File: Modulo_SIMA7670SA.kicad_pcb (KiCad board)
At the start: 2 copper layers, 100 x 78 mm, 58 parts, among them J1 TBP01R1-508-02BE, J2 DB9 Hembra Impreso 90°, J3 U.FL IPEX1 MALE, J4 SMA-J-P-X-RA-TH1, J5 Jack DC 2.1mm PCB recto, Q1 BSS138, Q2 FDN340P, Q3 FDN340P, Q4 BSS138, U1 MAX232, U2 24LC512, U3 BKP-A7670SA (Módulo SIMCOM), U4 MAX706, U5 Black_Pill_STM32F411CEUx, U6 LM2596S_Modulo_Regulable, U7 LM7805_TO220

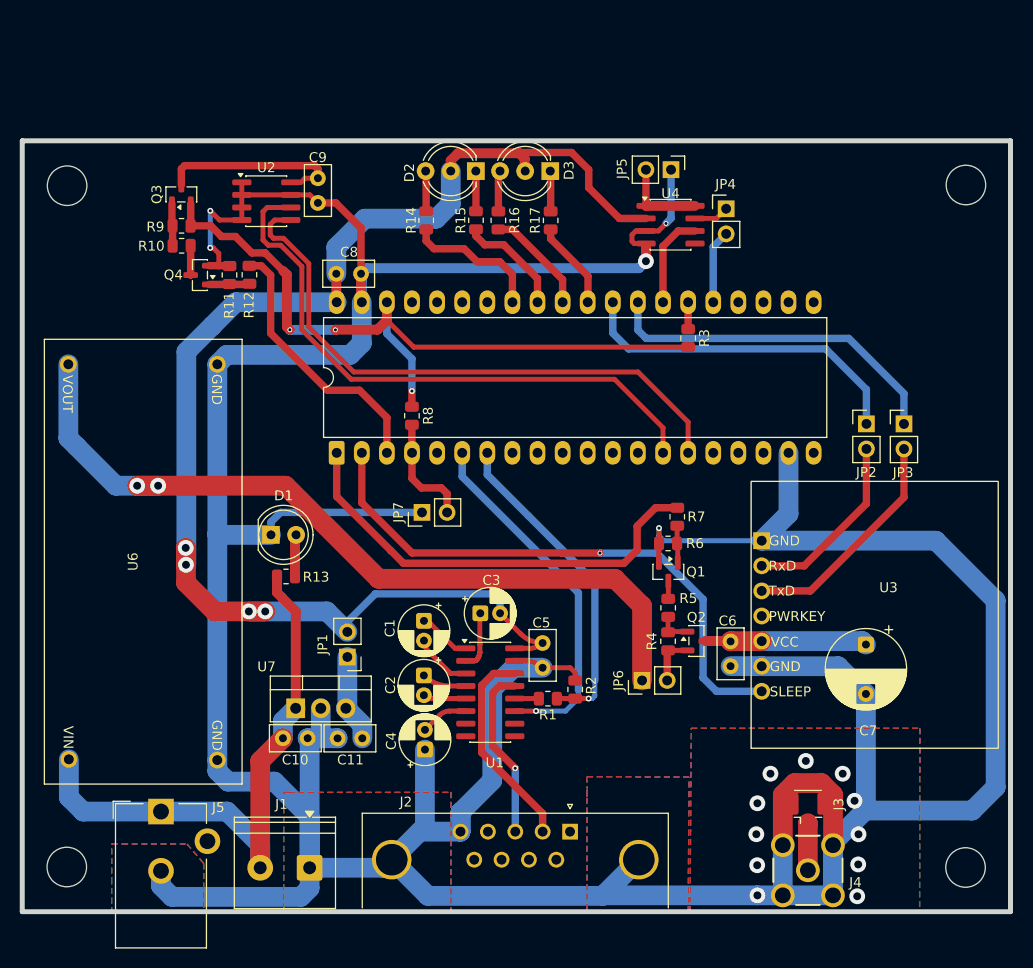
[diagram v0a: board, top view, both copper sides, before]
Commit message: Estamos haciendo un nuevo PCB porque se hicieron mpodificaciones en el circuito eléctrico para manejar la señal de ON/OFF del BKP-A7670SA en el riel de los 12V.
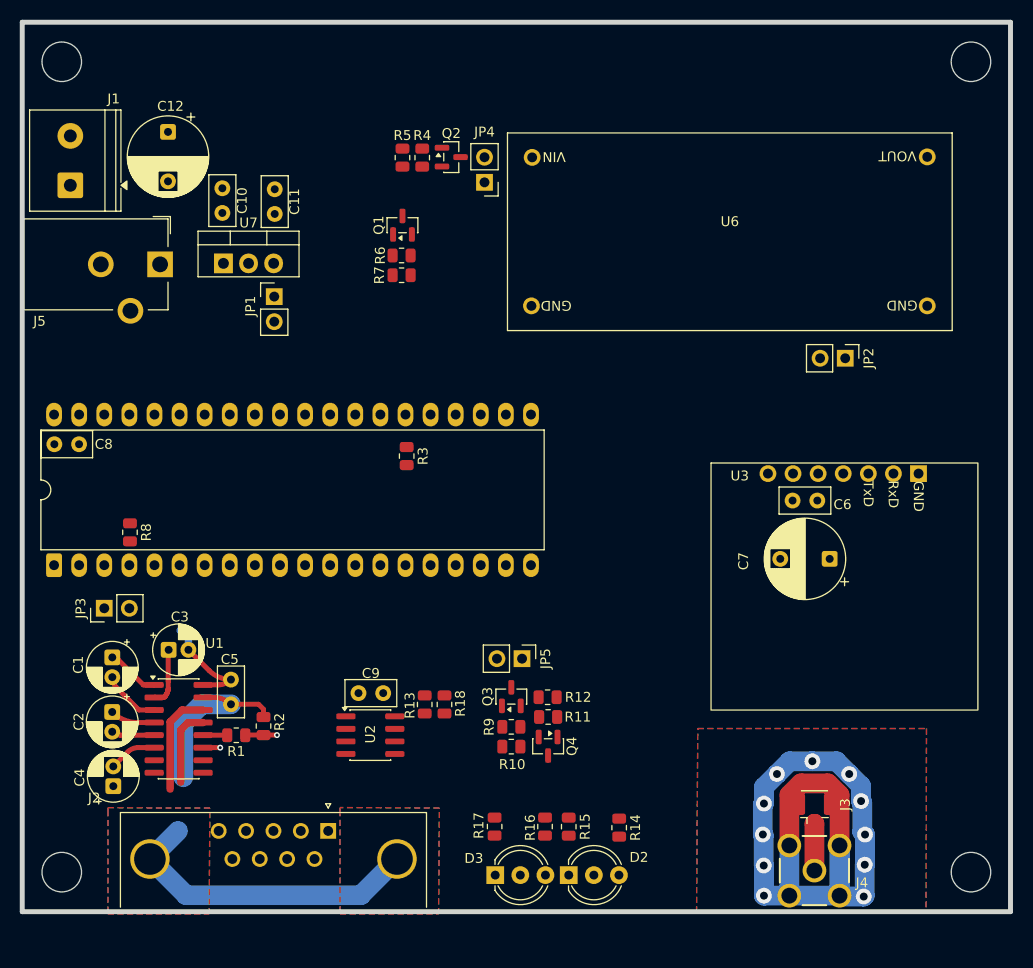
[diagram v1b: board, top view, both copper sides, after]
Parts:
- removed D1: LED Rojo 5mm, LED_THT:LED_D5.0mm
- removed JP6: Jumper_2_Open, Connector_PinHeader_2.54mm:PinHeader_1x02_P2.54mm_Vertical
- removed JP7: Config/Normal, Connector_PinHeader_2.54mm:PinHeader_1x02_P2.54mm_Vertical
- removed U4: MAX706, Package_SO:SOIC-8_3.9x4.9mm_P1.27mm
- added C12: 1000uF, Capacitor_THT:CP_Radial_D8.0mm_P5.00mm, F.Cu at (129.6, 66.8)
- added R18: 4K7, Resistor_SMD:R_0805_2012Metric, F.Cu at (157.6, 124.7)
- C7: value 1000uF -> 470uF
- JP3: value Jumper_2_Open -> Config/Normal
- R10: value 10K -> 3K3
- R4, R9: value 4K7 -> 10K
- R5: value 10K -> 15K
- moved JP3 83.0 mm to (123.2, 115.0), turned to 90 degrees
- moved J1 73.2 mm to (119.7, 72.2), turned to 90 degrees
- moved D2 71.9 mm to (170.2, 142.0), turned to 0 degrees
- moved D3 71.5 mm to (162.7, 142.0), turned to 0 degrees
- moved U6 68.1 mm to (186.5, 76.9), turned to 180 degrees
- moved R14 64.5 mm to (175.3, 137.2), turned to -90 degrees
- moved R15 62.1 mm to (170.2, 137.1), turned to -90 degrees
- moved R17 61.6 mm to (162.7, 137.0), turned to -90 degrees
- moved R16 61.5 mm to (167.8, 137.0), turned to -90 degrees
- moved Q3 60.8 mm to (164.3, 123.9)
- moved R9 60.7 mm to (164.3, 127.0)
- moved R10 60.7 mm to (164.3, 129.0)
- moved Q4 59.3 mm to (168.1, 128.9), turned to -90 degrees
- moved J5 55.4 mm to (128.8, 80.2), turned to -90 degrees
- moved R11 55.1 mm to (168.1, 126.0), turned to 180 degrees
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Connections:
- JP2 pad 2: UART2_RX -> 5V_MODEM
- JP3 pad 1: Net-(JP3-A) -> GND
- JP3 pad 2: UART2_TX -> Net-(JP3-B)
- JP4 pad 1: Net-(JP4-A) -> +12V
- JP4 pad 2: NRST -> 12V_StepDown
- JP5 pad 1: GND -> 3V3
- JP5 pad 2: Net-(JP5-B) -> 3V3_MEM
- Q2 pad 2: 5V_SWITCHING -> +12V
- Q2 pad 3: 5V_MODEM -> 12V_StepDown
- R13 pad 1: +12V -> 3V3_MEM
- R13 pad 2: Net-(D1-A) -> SCL I2C1
- R4 pad 1: 5V_SWITCHING -> +12V
- R8 pad 2: Net-(JP7-B) -> Net-(JP3-B)
- U3 pad 4: UART2_TX -> UART2_RX
- U3 pad 5: UART2_RX -> UART2_TX
- U5 pad 1: ON_MODEM -> unconnected-(U5-PB12-Pad1)
- U5 pad 16: unconnected-(U5-PB8-Pad16) -> ON_MEM
- U5 pad 17: unconnected-(U5-PB9-Pad17) -> SLEEP_MODEM
- U5 pad 18: unconnected-(U5-5V-Pad18) -> +5V
- U5 pad 2: SLEEP_MODEM -> unconnected-(U5-PB13-Pad2)
- U5 pad 20: unconnected-(U5-3V3-Pad20) -> 3V3
- U5 pad 25: NRST -> unconnected-(U5-~{NRST}-Pad25)
- U5 pad 27: WDT PULSE -> ON_MODEM
- U5 pad 28: Net-(JP3-A) -> UART2_TX
- U5 pad 29: Net-(JP2-A) -> UART2_RX
- U5 pad 3: ON_MEM -> unconnected-(U5-PB14-Pad3)
- U5 pad 4: Net-(JP7-B) -> Net-(JP3-B)
- U6 pad 1: +12V -> 12V_StepDown
- U6 pad 4: Net-(JP6-A) -> Net-(JP2-A)
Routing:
- net GND: track 475.3 -> 126.7 mm, vias 16 -> 11
- net +5V: track 139.6 -> 10.7 mm, vias 4 -> 0
- net Net-(JP6-A): track 82.2 -> 0.00 mm, vias 2 -> 0
- net 3V3: track 75.0 -> 0.00 mm, vias 3 -> 0
- net SCL I2C1: track 60.5 -> 0.00 mm
- net SDA I2C1: track 60.3 -> 0.00 mm
- net +12V: track 59.3 -> 0.00 mm
- net SLEEP_MODEM: track 58.1 -> 0.00 mm, vias 1 -> 0
- net ON_MODEM: track 45.5 -> 0.00 mm
- net Net-(JP3-A): track 35.5 -> 0.00 mm
- net UART1_TX: track 36.7 -> 1.74 mm
- net Net-(JP2-A): track 34.6 -> 0.00 mm
- net UART1_RX: track 33.1 -> 3.21 mm
- net ON_MEM: track 27.3 -> 0.00 mm
- net UART2_TX: track 23.2 -> 0.00 mm
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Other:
- board size 100 x 78 mm -> 100 x 90 mm
- board text removed: "GND"

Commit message: Adelantando algo del PCB. Fue ncesario modificar GPIOs del STM32 y renombrar rieles de 3.3V; 5V; y GND, para que no tengamos líneas sin rutear.
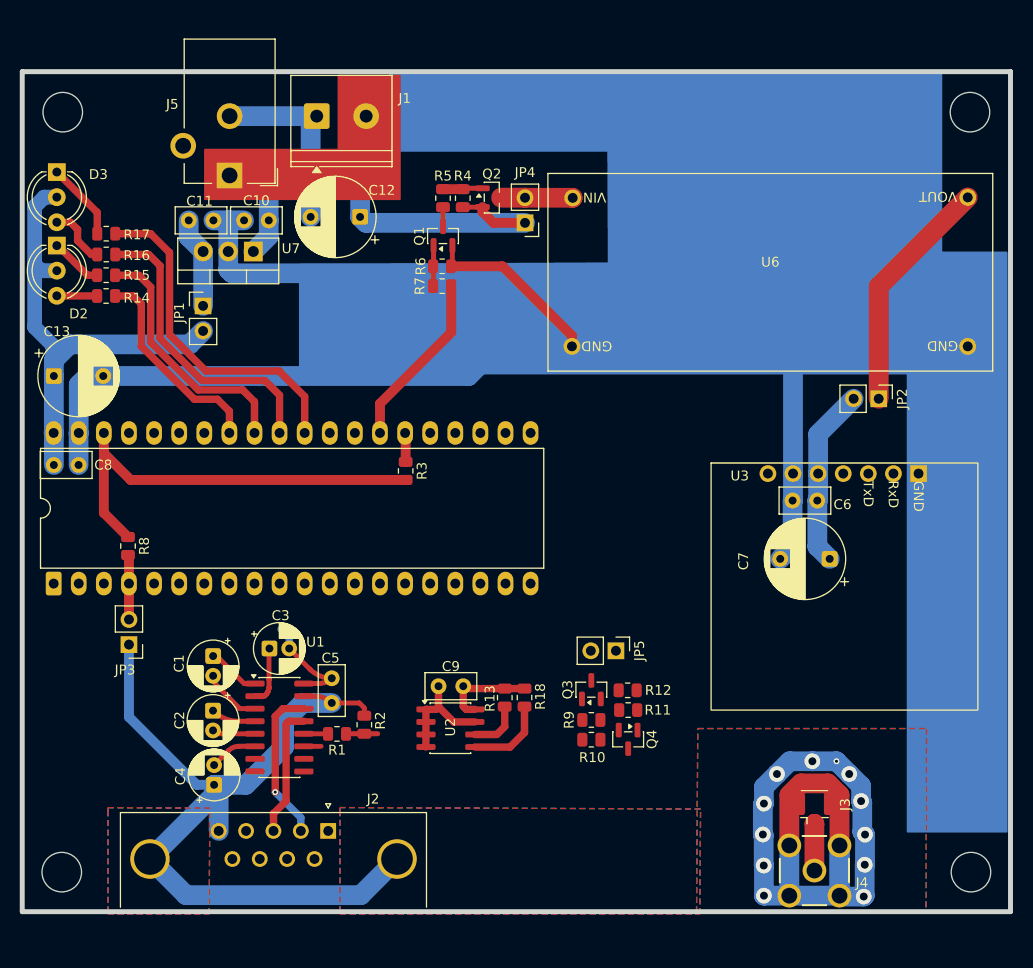
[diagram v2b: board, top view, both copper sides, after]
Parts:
- added C13: 470uF, Capacitor_THT:CP_Radial_D8.0mm_P5.00mm, F.Cu at (118.1, 91.5)
- moved D3 83.8 mm to (118.4, 70.8), turned to -90 degrees
- moved D2 82.1 mm to (118.4, 78.3), turned to -90 degrees
- moved R14 74.8 mm to (123.3, 83.4), turned to 180 degrees
- moved R16 73.0 mm to (123.4, 79.2), turned to 180 degrees
- moved R15 72.8 mm to (123.3, 81.3), turned to 180 degrees
- moved R17 71.7 mm to (123.4, 77.1), turned to 180 degrees
- moved J1 25.9 mm to (144.7, 65.2), turned to 0 degrees
- moved C12 21.3 mm to (149.0, 75.4), turned to 180 degrees
- moved J5 11.4 mm to (135.8, 71.2), turned to 180 degrees
- moved C1 10.2 mm to (134.2, 119.8)
- moved C5 10.2 mm to (146.2, 122.0)
- moved R1 10.2 mm to (146.7, 127.7)
- moved C4 10.2 mm to (134.3, 132.8)
- moved C2 10.2 mm to (134.2, 125.3)
- moved C3 10.2 mm to (139.9, 119.0)
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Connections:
- JP5 pad 1: 3V3 -> 3V3_b
- Q3 pad 2: 3V3 -> 3V3_b
- R9 pad 1: 3V3 -> 3V3_b
- U5 pad 20: 3V3 -> 3V3_b
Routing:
- net GND: track 126.7 -> 361.3 mm, vias 11 -> 12
- net +5V: track 10.7 -> 60.7 mm
- net +12V: track 0.00 -> 46.1 mm
- net 3V3: track 0.00 -> 43.2 mm
- net Net-(U5-PA4): track 0.00 -> 34.5 mm
- net Net-(U5-PA5): track 0.00 -> 30.6 mm
- net Net-(U5-PA6): track 0.00 -> 25.8 mm
- net Net-(JP2-A): track 0.00 -> 24.1 mm
- net Net-(U5-PA7): track 0.00 -> 21.1 mm
- net 5V_MODEM: track 0.00 -> 18.2 mm
- net ON_MODEM: track 0.00 -> 17.8 mm
- net 3V3_MEM: track 0.00 -> 9.64 mm
- net Net-(JP1-A): track 0.00 -> 9.26 mm
- net SDA I2C1: track 0.00 -> 8.26 mm
- net Net-(D3-K1): track 0.00 -> 8.02 mm
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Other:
- board size 100 x 90 mm -> 100 x 85 mm

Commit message: Se va avanzando con el PCB. Sin enrutar "17".
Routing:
- net +5V: track 60.7 -> 79.5 mm
- net Net-(Q3-G): track 0.00 -> 4.14 mm
- net Net-(Q4-G): track 0.00 -> 4.06 mm
- net Net-(Q4-D): track 0.00 -> 3.19 mm
- net 3V3_MEM: track 9.64 -> 12.7 mm
- net 3V3_b: track 0.00 -> 2.14 mm
- net GND: track 361.3 -> 363.3 mm
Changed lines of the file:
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@@
+	)
+	(segment
+		(start 172.4475 122.26)
+		(end 172.4475 119.3125)
+		(width 0.75)
+		(layer "F.Cu")
+		(net "3V3_MEM")
 	)
 	(segment
@@
 		(start 159.79 125.19)
 		(end 159.485 124.885)
+		(width 0.75)
+		(layer "F.Cu")
+		(net "3V3_MEM")
+	)
+	(segment
+		(start 172.4475 119.3125)
+		(end 172.395 119.26)
 		(width 0.75)
 		(layer "F.Cu")
@@
 	)
 	(segment
+		(start 175.2225 125.2975)
+		(end 175.26 125.26)
+		(width 0.75)
+		(layer "F.Cu")
+		(net "GND")
+	)
+	(segment
 		(start 158.385 80.235)
 		(end 158.26 80.36)
@@
 		(end 158.385 80.235)
 		(width 0.5)
+		(layer "F.Cu")
+		(net "GND")
+	)
+	(segment
+		(start 175.2225 127.285)
+		(end 175.2225 125.2975)
+		(width 0.75)
 		(layer "F.Cu")
 		(net "GND")
@@
 	)
 	(segment
+		(start 161.22 116.1)
+		(end 158.26 119.06)
+		(width 1.5)
+		(layer "B.Cu")
+		(net "+5V")
+	)
+	(segment
 		(start 131.8 88.26)
 		(end 119.66 88.26)
@@
 	)
 	(segment
-		(start 141.874888 119.03)
-		(end 141.874888 117.89863)
-		(width 0.75)
+		(start 149.16 119.06)
+		(end 146.18 122.04)
+		(width 1.5)
 		(layer "B.Cu")
 		(net "+5V")
@@
 	)
 	(segment
+		(start 161.22 112.46)
+		(end 161.22 116.1)
+		(width 1.5)
+		(layer "B.Cu")
+		(net "+5V")
+	)
+	(segment
 		(start 118.06 91.46)
 		(end 117.96 91.36)
@@
 	)
 	(segment
-		(start 141.874888 117.89863)
-		(end 141.041258 117.065)
-		(width 0.75)
+		(start 158.26 119.06)
+		(end 149.16 119.06)
+		(width 1.5)
 		(layer "B.Cu")
 		(net "+5V")
@@
 		(layer "F.Cu")
 		(net "Net-(U1-VS-)")
+	)
+	(segment
+		(start 171.4975 126.2225)
+		(end 171.535 126.26)
+		(width 0.75)
+		(layer "F.Cu")
+		(net "Net-(Q3-G)")
+	)
+	(segment
+		(start 171.535 128.26)
+		(end 171.535 126.26)
+		(width 0.75)
+		(layer "F.Cu")
+		(net "Net-(Q3-G)")
+	)
+	(segment
+		(start 171.4975 124.135)
+		(end 171.4975 126.2225)
+		(width 0.75)
+		(layer "F.Cu")
+		(net "Net-(Q3-G)")
 	)
 	(segment
@@
 	)
 	(segment
-		(start 125.66 116.16)
-		(end 125.66 112.46)
-		(width 1)
-		(layer "F.Cu")
-		(net "Net-(JP3-B)")
-	)
-	(segment
 		(start 125.66 112.46)
 		(end 125.66 109.6725)
@@
 	)
 	(segment
+		(start 125.66 116.095)
+		(end 125.66 112.46)
+		(width 0.75)
+		(layer "B.Cu")
+		(net "Net-(JP3-B)")
+	)
+	(segment
 		(start 145.095 128.93)
 		(end 143.36 128.93)
@@
 		(layer "F.Cu")
 		(net "Net-(U1-VS+)")
+	)
+	(segment
+		(start 177.035 125.21)
+		(end 177.085 125.26)
+		(width 0.75)
+		(layer "F.Cu")
+		(net "Net-(Q4-G)")
+	)
+	(segment
+		(start 177.085 125.26)
+		(end 177.085 127.2475)
+		(width 0.75)
+		(layer "F.Cu")
+		(net "Net-(Q4-G)")
+	)
+	(segment
+		(start 177.035 123.26)
+		(end 177.035 125.21)
+		(width 0.75)
+		(layer "F.Cu")
+		(net "Net-(Q4-G)")
+	)
+	(segment
+		(start 177.085 127.2475)
+		(end 177.1225 127.285)
+		(width 0.75)
+		(layer "F.Cu")
+		(net "Net-(Q4-G)")
 	)
 	(segment
@@
 	)
 	(segment
+		(start 174.26 129.16)
+		(end 176.1725 129.16)
+		(width 0.75)
+		(layer "F.Cu")
+		(net "Net-(Q4-D)")
+	)
+	(segment
+		(start 173.36 128.26)
+		(end 174.26 129.16)
+		(width 0.75)
+		(layer "F.Cu")
+		(net "Net-(Q4-D)")
+	)
+	(segment
 		(start 157.435 74.3725)
 		(end 157.435 76.36)
@@
 		(net "Net-(Q1-D)")
 	)
+	(segment
+		(start 173.3975 126.2225)
+		(end 173.36 126.26)
+		(width 0.75)
+		(layer "F.Cu")
+		(net "3V3_b")
+	)
+	(segment
+		(start 173.3975 124.135)
+		(end 173.3975 126.2225)
+		(width 0.75)
+		(layer "F.Cu")
+		(net "3V3_b")
+	)
 	(zone

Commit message: Ya está todo ruteado, falta una sola net sin rutear que no se cual es. Solo hay que revisar.
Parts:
- moved R18 10.1 mm to (156.1, 120.7), turned to 0 degrees
- moved R11 9.62 mm to (175.3, 115.7)
- moved R12 9.62 mm to (175.3, 113.7)
- moved Q4 9.62 mm to (175.3, 118.6)
- moved JP5 8.63 mm to (166.3, 120.0), turned to 0 degrees
- moved R13 7.71 mm to (156.1, 122.7), turned to 0 degrees
- moved R10 6.43 mm to (175.3, 122.5), turned to 90 degrees
- moved C9 6.08 mm to (154.9, 126.9), turned to -90 degrees
- moved R9 3.84 mm to (173.3, 122.5), turned to -90 degrees
- moved JP3 3.57 mm to (128.2, 116.2), turned to -90 degrees
- moved Q3 2.27 mm to (170.3, 122.5), turned to 180 degrees
- moved U2 1.48 mm to (159.2, 128.2), turned to 90 degrees
- moved R1 0.57 mm to (146.5, 127.2)
- moved R2 0.54 mm to (149.3, 126.2)
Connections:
- C3 pad 2: +5V -> +5V_b
- C5 pad 1: +5V -> +5V_b
- J2 pad 0: (no net) -> GND
- U1 pad 16: +5V -> +5V_b
- U5 pad 18: +5V -> +5V_b
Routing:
- net GND: track 363.3 -> 441.0 mm, vias 12 -> 13
- net UART2_RX: track 0.00 -> 61.2 mm, vias 0 -> 1
- net UART2_TX: track 0.00 -> 59.9 mm, vias 0 -> 1
- net SLEEP_MODEM: track 0.00 -> 39.5 mm
- net UART1_TX: track 1.73 -> 39.9 mm, vias 0 -> 1
- net +5V_b: track 0.00 -> 30.7 mm
- net +5V: track 79.5 -> 50.0 mm
- net UART1_RX: track 3.21 -> 30.3 mm
- net ON_MEM: track 0.00 -> 20.7 mm
- net SCL I2C1: track 5.38 -> 19.2 mm, vias 0 -> 2
- net 3V3_MEM: track 12.7 -> 25.8 mm
- net 3V3_b: track 2.14 -> 15.2 mm
- net SDA I2C1: track 8.26 -> 17.9 mm
- net Net-(Q4-D): track 3.19 -> 2.04 mm

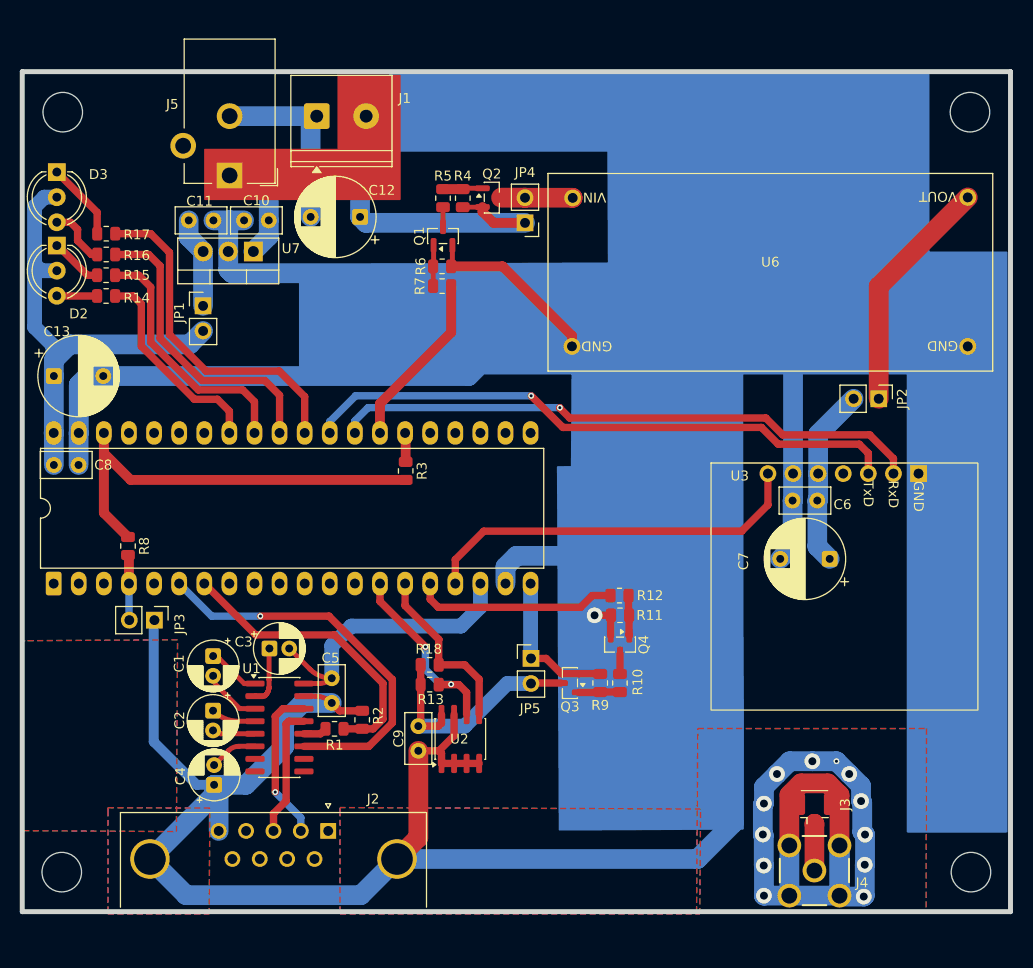
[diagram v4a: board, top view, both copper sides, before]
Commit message: fix(pcb): corregir jerarquia de prioridades en zonas de cobre
- Reordenar prioridades de las 10 zonas: potencia (+12V, Net-JP2-A)
  por debajo del plano de GND, GND en rango 4-8, zona RF_LTE_4G
  como techo absoluto en prioridad 9
- Restaurar nombre descriptivo "RF_LTE_4G" (habia quedado
  renombrada a "Pour0"/"Pour1" con uuid duplicado por error previo)
- Subir Pour3 (GND) de prioridad 1 a 4+, unico outlier que quedaba
  por debajo de los pours de potencia

Nota de diseno: se dejan documentadas 8 superposiciones de courtyard
(C6/C7-U3, C8/R3/R8-U5, D3-H2, C4-J2, C9-R13) como no criticas -
los componentes involucrados (U3, U5) montan sobre zocalo con
altura libre suficiente debajo. Excluir estas violaciones puntuales
en el DRC de KiCad (click derecho -> Exclude this violation) para
mantener el resto de las verificaciones limpias.
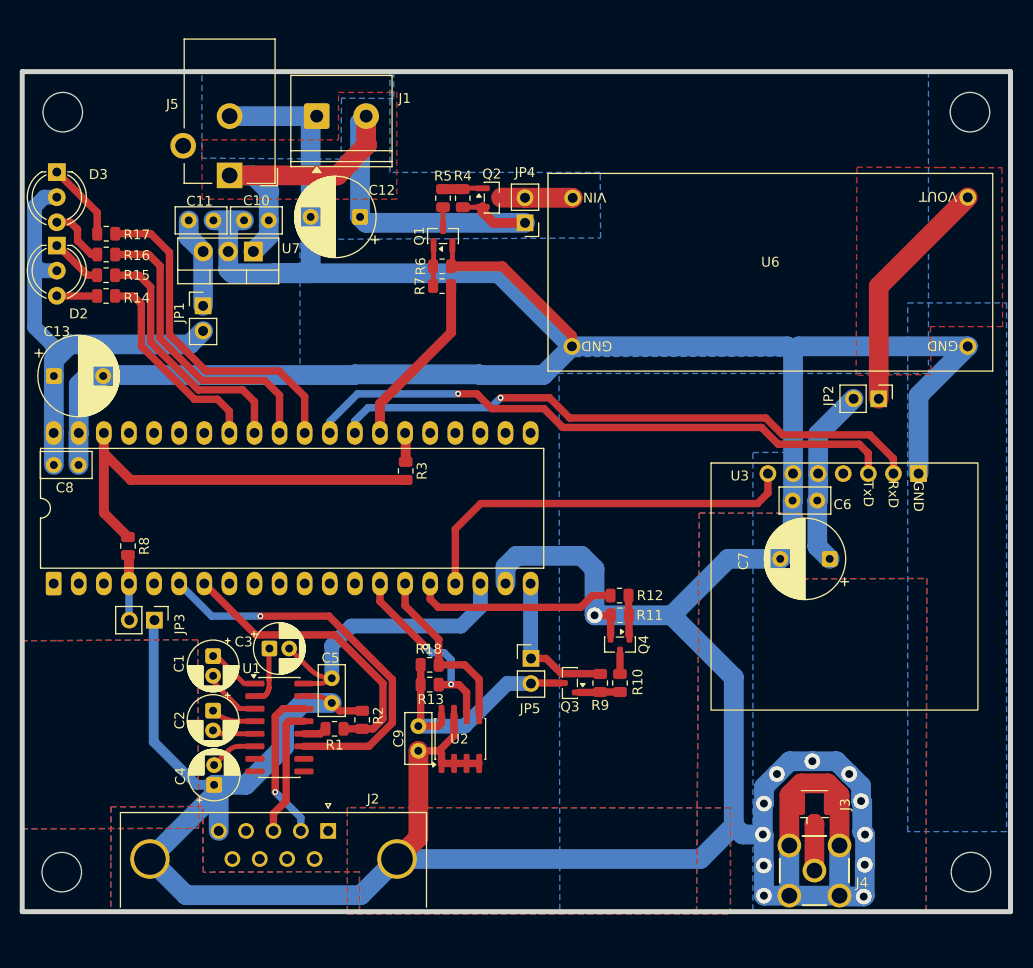
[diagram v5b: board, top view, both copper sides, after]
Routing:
- net GND: track 441.0 -> 520.4 mm, vias 13 -> 12
- net +12V: track 46.1 -> 64.3 mm
- net SLEEP_MODEM: track 39.5 -> 40.6 mm
- net UART2_TX: track 59.9 -> 60.7 mm
- added copper zone on F.Cu, net +12V
- added copper zone on F.Cu, net Net-(JP2-A)
